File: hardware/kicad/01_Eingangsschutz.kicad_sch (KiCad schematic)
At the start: 0 parts

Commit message: hardware(power): retire dead relay ACC and duplicate latch/RC alternatives; preserve 555 timeout study
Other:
- removed sheet 01B ACC-Start und HOLD-OR (vorlaeufig)
- removed sheet 01E ACC-OFF hardware latch (isolierter Vorentwurf)
- removed sheet 01F RC-Selbstabschaltung (preiswerter Versuch)
- note added: "01D LM74930 ALTSTAND NICHT MEHR AKTIV; 01G KOSTENSPAR-SCHUTZ TEILENTWURF. 01A RELAIS-AUX 5V AUS AKTIVER HIERARCHIE ENTFERNT; 01B RELAIS-EINSCHALTSTUFE UND 01E/01F ALTERNATIVEN AUS AKTIVER HIERARCHIE ENTFERNT. 01C 555-NACHLAUF VORLAEUFIG, BUCK_ENABLE NOCH NICHT ANGESCHLOSSEN."
- note removed: "01D LM74930 ALTSTAND NICHT MEHR AKTIV; 01G KOSTENSPAR-SCHUTZ TEILENTWURF. 01A RELAIS-AUX 5V AUS AKTIVER HIERARCHIE ENTFERNT; 01B/01C ALTE ENTWURFE. 01E / 01F NOCH NICHT ANGEKOPPELTE HOLD-KANDIDATEN."
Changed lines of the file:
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@@
 (title_block (title "TripTracer V1 - Automotive Eingangsschutz, relayless design") (date "2026-10-14") (rev "LMR38020 MAIN BUCK / LEGACY CIRCUITS NOT APPROVED"))
 (text "RELAIS K101 UND ALTE RELAIS-STROMPFAD-TOPOLOGIE AUS DEM AKTIVEN SCHALTPLAN ENTFERNT; ALTSTAND IN GIT-HISTORIE." (at 191 58 0) (effects (font (size 1.7 1.7))))
-(text "01D LM74930 ALTSTAND NICHT MEHR AKTIV; 01G KOSTENSPAR-SCHUTZ TEILENTWURF. 01A RELAIS-AUX 5V AUS AKTIVER HIERARCHIE ENTFERNT; 01B/01C ALTE ENTWURFE. 01E / 01F NOCH NICHT ANGEKOPPELTE HOLD-KANDIDATEN." (at 191 73 0) (effects (font (size 1.5 1.5))))
-(sheet (at 214 257) (size 175 28) (exclude_from_sim no) (in_bom yes) (on_board yes) (dnp no)
- (stroke (width 0) (type solid)) (fill (color 0 0 0 0))
- (property "Sheetname" "01B ACC-Start und HOLD-OR (vorlaeufig)" (at 214 256.24 0) (effects (font (size 1.524 1.524)) (justify left bottom)))
- (property "Sheetfile" "01B_ACC_WAKE.kicad_sch" (at 214 285.76 0) (effects (font (size 1.524 1.524)) (justify left top)))
- (instances (project "TripTracer_V1" (path "/a26d9b0c-7f10-4e5a-a65f-000000000064/a26d9b0c-7f10-4e5a-a65f-000000000065" (page "2.2"))))
-)
+(text "01D LM74930 ALTSTAND NICHT MEHR AKTIV; 01G KOSTENSPAR-SCHUTZ TEILENTWURF. 01A RELAIS-AUX 5V AUS AKTIVER HIERARCHIE ENTFERNT; 01B RELAIS-EINSCHALTSTUFE UND 01E/01F ALTERNATIVEN AUS AKTIVER HIERARCHIE ENTFERNT. 01C 555-NACHLAUF VORLAEUFIG, BUCK_ENABLE NOCH NICHT ANGESCHLOSSEN." (at 191 73 0) (effects (font (size 1.5 1.5))))
 (sheet (at 25 290) (size 155 28) (exclude_from_sim no) (in_bom yes) (on_board yes) (dnp no)
 (stroke (width 0) (type solid)) (fill (color 0 0 0 0))
@@
  (instances (project "TripTracer_V1" (path "/a26d9b0c-7f10-4e5a-a65f-000000000064/a26d9b0c-7f10-4e5a-a65f-000000000065" (page "2.4"))))
 )
-(sheet (at 25 328.93) (size 185.42 27.94) (exclude_from_sim no) (in_bom yes) (on_board yes) (dnp no)
- (stroke (width 0) (type solid)) (fill (color 0 0 0 0))
- (property "Sheetname" "01E ACC-OFF hardware latch (isolierter Vorentwurf)" (at 25 328.17 0) (effects (font (size 1.524 1.524)) (justify left bottom)))
- (property "Sheetfile" "01E_OFF_LATCH.kicad_sch" (at 25 357.63 0) (effects (font (size 1.524 1.524)) (justify left top)))
- (instances (project "TripTracer_V1" (path "/a26d9b0c-7f10-4e5a-a65f-000000000064/a26d9b0c-7f10-4e5a-a65f-000000000065" (page "2.5"))))
-)
-(sheet (at 226.06 328.93) (size 185.42 27.94) (exclude_from_sim no) (in_bom yes) (on_board yes) (dnp no)
- (stroke (width 0) (type solid)) (fill (color 0 0 0 0))
- (property "Sheetname" "01F RC-Selbstabschaltung (preiswerter Versuch)" (at 226.06 328.17 0) (effects (font (size 1.524 1.524)) (justify left bottom)))
- (property "Sheetfile" "01F_RC_SHUTDOWN.kicad_sch" (at 226.06 357.63 0) (effects (font (size 1.524 1.524)) (justify left top)))
- (instances (project "TripTracer_V1" (path "/a26d9b0c-7f10-4e5a-a65f-000000000064/a26d9b0c-7f10-4e5a-a65f-000000000065" (page "2.6"))))
-)
 (sheet_instances (path "/" (page "2")))

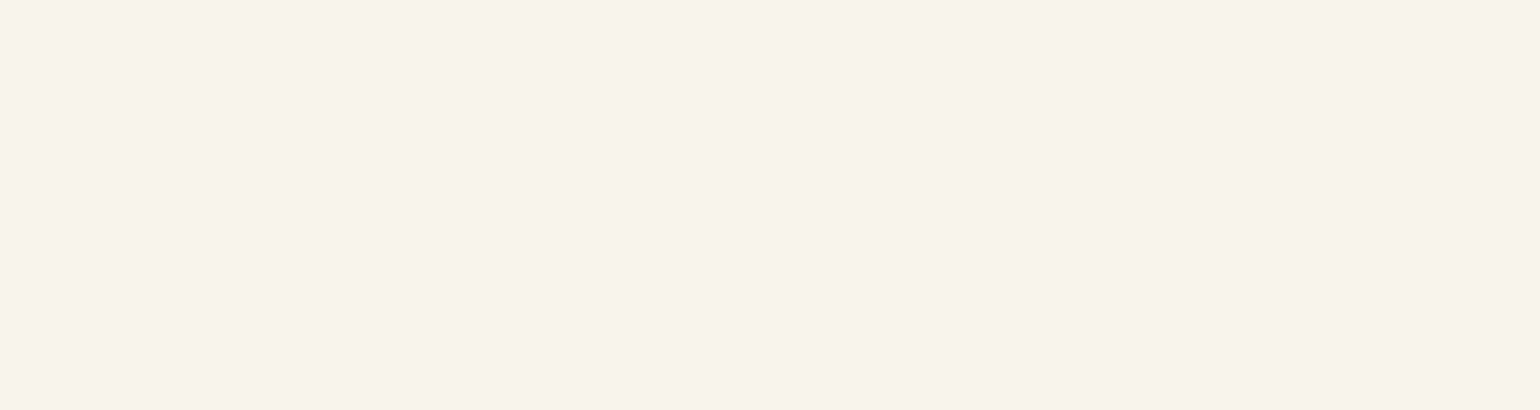
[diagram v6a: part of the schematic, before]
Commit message: hardware(power): activate optoisolated ACC cold-start/HOLD gate in root KiCad schematic
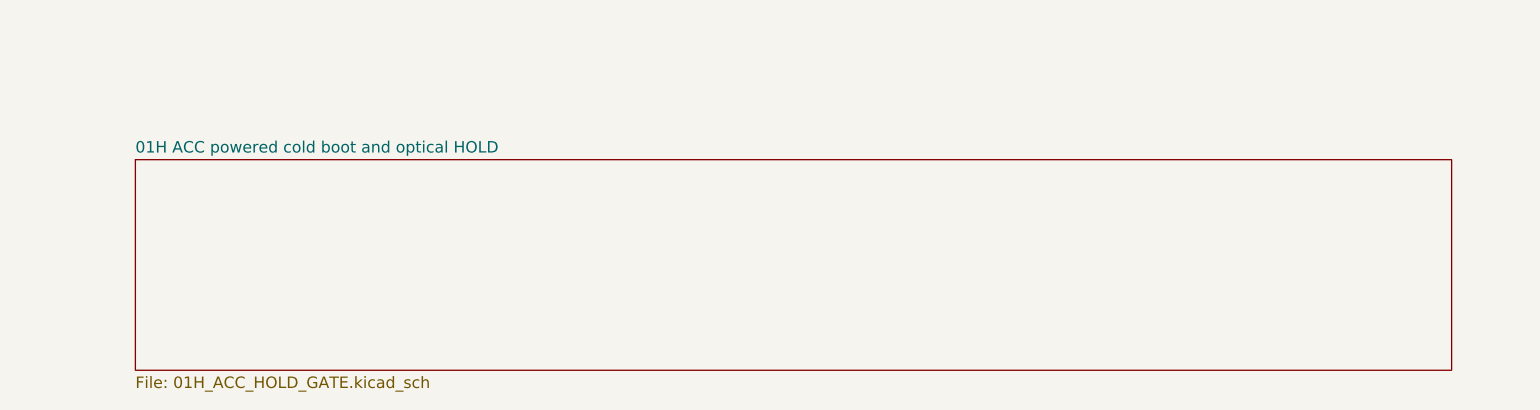
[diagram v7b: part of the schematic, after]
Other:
- added sheet 01H ACC powered cold boot and optical HOLD (01H_ACC_HOLD_GATE.kicad_sch)
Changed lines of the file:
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@@
  (instances (project "TripTracer_V1" (path "/a26d9b0c-7f10-4e5a-a65f-000000000064/a26d9b0c-7f10-4e5a-a65f-000000000065" (page "2.4"))))
+)
+(sheet (at 214 367) (size 175 28) (exclude_from_sim no) (in_bom yes) (on_board yes) (dnp no)
+ (stroke (width 0) (type solid)) (fill (color 0 0 0 0))
+ (property "Sheetname" "01H ACC powered cold boot and optical HOLD" (at 214 366.24 0) (effects (font (size 1.524 1.524)) (justify left bottom)))
+ (property "Sheetfile" "01H_ACC_HOLD_GATE.kicad_sch" (at 214 395.76 0) (effects (font (size 1.524 1.524)) (justify left top)))
+ (instances (project "TripTracer_V1" (path "/a26d9b0c-7f10-4e5a-a65f-000000000064/a26d9b0c-7f10-4e5a-a65f-000000000065" (page "2.7"))))
 )
 (sheet_instances (path "/" (page "2")))

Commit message: wire LM74800 protection sheet into active TripTracer hierarchy; retire legacy 01G from netlist
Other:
- sheet 01G einfache BAT-Eingangsstufe D901/D902 (LABOR) renamed 01I LM74800-Q1 FET Eingangsschutz (WIP)
- sheet 01I LM74800-Q1 FET Eingangsschutz (WIP): file 01G_SIMPLE_INPUT.kicad_sch -> 01I_LM74800_INPUT.kicad_sch
- note added: "01D LM74930 und 01G S5MC/TVS5800 bleiben INAKTIVE Vergleichsstaende. Neu aktiv: 01I LM74800-Q1 COMMON SOURCE; nicht freigegeben. 01A RELAIS-AUX 5V AUS AKTIVER HIERARCHIE ENTFERNT; 01B RELAIS-EINSCHALTSTUFE UND 01E/01F ALTERNATIVEN AUS AKTIVER HIERARCHIE ENTFERNT. 01C 555-NACHLAUF VORLAEUFIG, BUCK_ENABLE NOCH NICHT ANGESCHLOSSEN."
- note removed: "01D LM74930 ALTSTAND NICHT MEHR AKTIV; 01G KOSTENSPAR-SCHUTZ TEILENTWURF. 01A RELAIS-AUX 5V AUS AKTIVER HIERARCHIE ENTFERNT; 01B RELAIS-EINSCHALTSTUFE UND 01E/01F ALTERNATIVEN AUS AKTIVER HIERARCHIE ENTFERNT. 01C 555-NACHLAUF VORLAEUFIG, BUCK_ENABLE NOCH NICHT ANGESCHLOSSEN."
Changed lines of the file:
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@@
 (title_block (title "TripTracer V1 - Automotive Eingangsschutz, relayless design") (date "2026-10-14") (rev "LMR38020 MAIN BUCK / LEGACY CIRCUITS NOT APPROVED"))
 (text "RELAIS K101 UND ALTE RELAIS-STROMPFAD-TOPOLOGIE AUS DEM AKTIVEN SCHALTPLAN ENTFERNT; ALTSTAND IN GIT-HISTORIE." (at 191 58 0) (effects (font (size 1.7 1.7))))
-(text "01D LM74930 ALTSTAND NICHT MEHR AKTIV; 01G KOSTENSPAR-SCHUTZ TEILENTWURF. 01A RELAIS-AUX 5V AUS AKTIVER HIERARCHIE ENTFERNT; 01B RELAIS-EINSCHALTSTUFE UND 01E/01F ALTERNATIVEN AUS AKTIVER HIERARCHIE ENTFERNT. 01C 555-NACHLAUF VORLAEUFIG, BUCK_ENABLE NOCH NICHT ANGESCHLOSSEN." (at 191 73 0) (effects (font (size 1.5 1.5))))
+(text "01D LM74930 und 01G S5MC/TVS5800 bleiben INAKTIVE Vergleichsstaende. Neu aktiv: 01I LM74800-Q1 COMMON SOURCE; nicht freigegeben. 01A RELAIS-AUX 5V AUS AKTIVER HIERARCHIE ENTFERNT; 01B RELAIS-EINSCHALTSTUFE UND 01E/01F ALTERNATIVEN AUS AKTIVER HIERARCHIE ENTFERNT. 01C 555-NACHLAUF VORLAEUFIG, BUCK_ENABLE NOCH NICHT ANGESCHLOSSEN." (at 191 73 0) (effects (font (size 1.5 1.5))))
 (sheet (at 25 290) (size 155 28) (exclude_from_sim no) (in_bom yes) (on_board yes) (dnp no)
 (stroke (width 0) (type solid)) (fill (color 0 0 0 0))
@@
 (sheet (at 214 290) (size 175 28) (exclude_from_sim no) (in_bom yes) (on_board yes) (dnp no)
  (stroke (width 0) (type solid)) (fill (color 0 0 0 0))
- (property "Sheetname" "01G einfache BAT-Eingangsstufe D901/D902 (LABOR)" (at 214 289.24 0) (effects (font (size 1.524 1.524)) (justify left bottom)))
- (property "Sheetfile" "01G_SIMPLE_INPUT.kicad_sch" (at 214 318.76 0) (effects (font (size 1.524 1.524)) (justify left top)))
+ (property "Sheetname" "01I LM74800-Q1 FET Eingangsschutz (WIP)" (at 214 289.24 0) (effects (font (size 1.524 1.524)) (justify left bottom)))
+ (property "Sheetfile" "01I_LM74800_INPUT.kicad_sch" (at 214 318.76 0) (effects (font (size 1.524 1.524)) (justify left top)))
  (instances (project "TripTracer_V1" (path "/a26d9b0c-7f10-4e5a-a65f-000000000064/a26d9b0c-7f10-4e5a-a65f-000000000065" (page "2.4"))))
 )
